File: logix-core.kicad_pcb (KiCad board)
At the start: 6 copper layers, 100 x 80 mm, 238 parts, among them J1 QSH-030-01-X-D-A-XX, J2 QSH-030-01-X-D-A-XX, J3 878321420, Q1 TPNTK3139PT1G, Q10 TPNTK3139PT1G, Q11 2N7002M3T5G-ES, Q12 2N7002M3T5G-ES, Q13 2N7002M3T5G-ES, Q14 2N7002M3T5G-ES, Q15 2N7002M3T5G-ES, Q16 2N7002M3T5G-ES, Q17 2N7002M3T5G-ES, Q18 2N7002M3T5G-ES, Q19 TPNTK3139PT1G, Q2 2N7002M3T5G-ES, Q20 2N7002M3T5G-ES, Q21 2N7002M3T5G-ES, Q22 2N7002M3T5G-ES, Q23 2N7002M3T5G-ES, Q24 2N7002M3T5G-ES, Q25 2N7002M3T5G-ES, Q26 2N7002M3T5G-ES, Q27 2N7002M3T5G-ES, Q3 2N7002M3T5G-ES, Q4 2N7002M3T5G-ES, Q5 2N7002M3T5G-ES, Q6 2N7002M3T5G-ES, Q7 2N7002M3T5G-ES, Q8 2N7002M3T5G-ES, Q9 2N7002M3T5G-ES, SW1 SMXS-04K-TP, SW2 TS-1187A-B-A-B, SW3 TS-1187A-B-A-B, SW4 TS-1187A-B-A-B, U1 XC7A35T-FGG484, U2 MP5470GL-0000-P, U3 TPUSBLC6-4SC6, U4 FT230XQ, U5 MX25L3233FZN, U6 MT41K256M16TW-107:P

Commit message: did alot of stuff
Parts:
- C1, C14, C15, C28, C29, C42, C43, C65, C71, C81: footprint Capacitor_SMD:C_1210_3225Metric -> Capacitor_SMD:C_1206_3216Metric
- R1, R10, R11, R12, R13, R14, R15, R16, R2, R3, R4, R5, R6, R8, R9: footprint Resistor_SMD:R_0402_1005Metric_Pad0.72x0.64mm_HandSolder -> Resistor_SMD:R_0402_1005Metric
- R20: footprint Capacitor_SMD:C_0402_1005Metric -> Resistor_SMD:R_0402_1005Metric
- moved C71 18.0 mm to (140.5, 108.8), turned to 90 degrees
- moved C43 12.0 mm to (173.8, 107.5)
- moved C53 6.15 mm to (126.0, 125.5), turned to -90 degrees
- moved R11 5.71 mm to (125.2, 117.2), turned to 90 degrees
- moved R13 5.26 mm to (125.2, 120.2), turned to -90 degrees
- moved C1 5.14 mm to (178.5, 108.2), turned to 90 degrees
- moved R14 4.10 mm to (128.5, 128.8)
- moved FB1 2.47 mm to (122.2, 115.2)
- moved C14 2.01 mm to (173.8, 104.0)
- moved C8 1.90 mm to (172.2, 101.5)
- moved C9 1.75 mm to (172.2, 100.2)
- moved C13 1.60 mm to (172.2, 99.0)
- moved Q20 1.50 mm to (208.2, 80.0)
- moved Q22 1.50 mm to (209.8, 80.0)
- moved R56 1.50 mm to (208.2, 82.2)
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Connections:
- net Net-(USB1-VCC) renamed /USB/EXT_VBUS
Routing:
- net GND: track 0.00 -> 73.0 mm, vias 0 -> 184
- net (no net): track 0.00 -> 52.7 mm, vias 0 -> 35
- net /DDR3_DQ15: track 0.00 -> 38.4 mm, vias 0 -> 2
- net /DDR3_ADDR8: track 0.00 -> 36.6 mm, vias 0 -> 2
- net /DDR3_UDQS+: track 0.00 -> 36.5 mm, vias 0 -> 2
- net /DDR3_ADDR13: track 0.00 -> 36.4 mm, vias 0 -> 2
- net /DDR3_UDQS-: track 0.00 -> 36.4 mm, vias 0 -> 2
- net /DDR3_ADDR12: track 0.00 -> 34.4 mm, vias 0 -> 2
- net /DDR3_ADDR10: track 0.00 -> 33.6 mm, vias 0 -> 2
- net /DDR3_ADDR11: track 0.00 -> 33.3 mm, vias 0 -> 2
- net /DDR3_DQ10: track 0.00 -> 32.2 mm, vias 0 -> 2
- net /DDR3_ADDR14: track 0.00 -> 31.8 mm, vias 0 -> 2
- net /DDR3_DQ12: track 0.00 -> 31.0 mm, vias 0 -> 2
- net /DDR3_DQ14: track 0.00 -> 30.7 mm, vias 0 -> 2
- net /DDR3_DQ8: track 0.00 -> 29.6 mm, vias 0 -> 2
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- added copper zone on B.Cu, net /FPGA/FPGA pg.1/VCCO13
- added copper zone on F.Cu, net /FPGA/FPGA pg.1/VCCO13
- added copper zone on B.Cu, net /FPGA/FPGA pg.1/VCCO14
- added copper zone on F.Cu, net /FPGA/FPGA pg.1/VCCO14
- added copper zone on B.Cu, net /FPGA/FPGA pg.2/VCCO15
- added copper zone on F.Cu, net /FPGA/FPGA pg.2/VCCO15
- added copper zone on B.Cu, net /FPGA/FPGA pg.2/VCCO16
- added copper zone on F.Cu, net /FPGA/FPGA pg.2/VCCO16
- added copper zone on B.Cu, net /FPGA/FPGA pg.3/VCCO34
- added copper zone on F.Cu, net /FPGA/FPGA pg.3/VCCO34
- added copper zone on B.Cu, net /FPGA/FPGA pg.3/VCCO35
- added copper zone on F.Cu, net /FPGA/FPGA pg.3/VCCO35
- added copper zone on B.Cu, net /FPGA/FPGA pg.4/VCCO_0
- added copper zone on F.Cu, net /FPGA/FPGA pg.4/VCCO_0
- added copper zone on B.Cu, net /FPGA/FPGA pg.5/MGTAVCC
- added copper zone on F.Cu, net /FPGA/FPGA pg.5/MGTAVCC
- added copper zone on B.Cu, net /FPGA/FPGA pg.5/MGTAVTT
- added copper zone on F.Cu, net /FPGA/FPGA pg.5/MGTAVTT
- added copper zone on B.Cu, net /FPGA/FPGA pg.5/VCCADC
- added copper zone on F.Cu, net /FPGA/FPGA pg.5/VCCADC
- added copper zone on B.Cu, net /FPGA/FPGA pg.5/VCCAUX
- added copper zone on F.Cu, net /FPGA/FPGA pg.5/VCCAUX
- added copper zone on B.Cu, net /FPGA/FPGA pg.5/VCCBRAM
- added copper zone on F.Cu, net /FPGA/FPGA pg.5/VCCBRAM
- added copper zone on B.Cu, net /FPGA/FPGA pg.5/VCCINT
- added copper zone on F.Cu, net /FPGA/FPGA pg.5/VCCINT
- added copper zone on F.Cu, net /USB/EXT_VBUS
- added copper zone on B.Cu, net GND
- added copper zone on F.Cu, net GND
- removed copper zone on In4.Cu, net +1V5

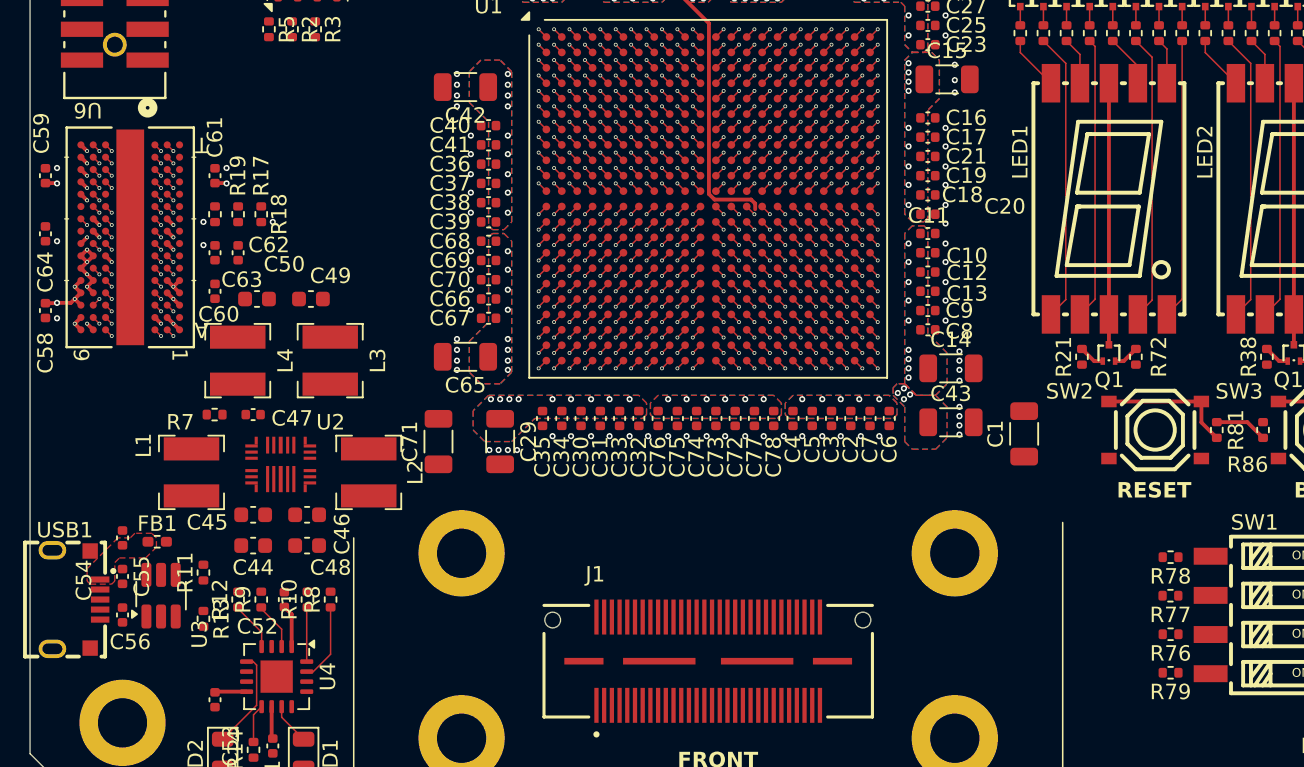
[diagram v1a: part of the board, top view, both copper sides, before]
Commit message: did a bit of ddr routing
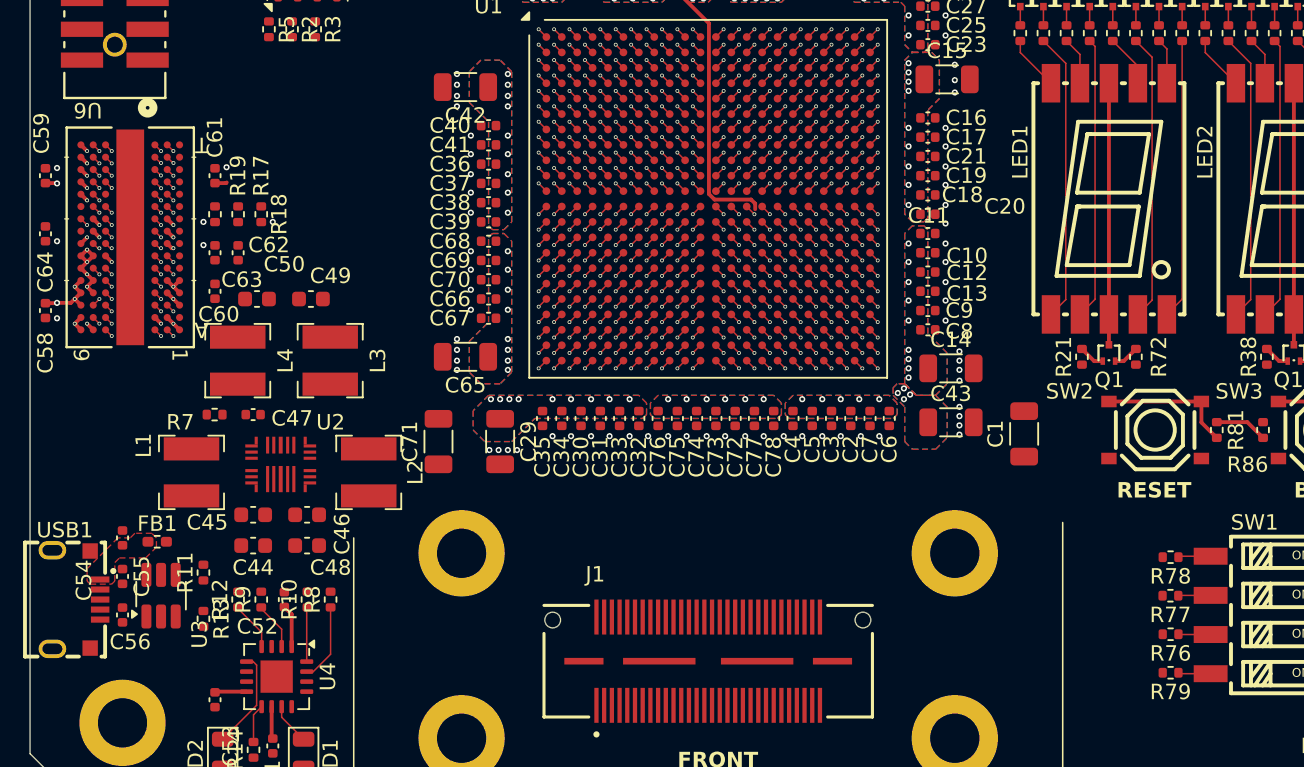
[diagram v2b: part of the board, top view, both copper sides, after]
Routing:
- net /DDR3_BLOCK_ADDR1: track 1.27 -> 42.0 mm
- net /DDR3_LDQS-: track 1.27 -> 40.7 mm
- net /DDR3_DQ7: track 1.27 -> 38.5 mm
- net /DDR3_LDQS+: track 1.27 -> 37.5 mm
- net /DDR3_CLK_EN: track 1.27 -> 36.6 mm
- net /DDR3_DQ5: track 1.27 -> 36.5 mm
- net /DDR3_ADDR4: track 1.27 -> 34.9 mm
- net /DDR3_BLOCK_ADDR2: track 1.27 -> 34.1 mm
- net /DDR3_ADDR6: track 1.27 -> 33.7 mm
- net /DDR3_DQ3: track 1.27 -> 32.5 mm
- net /DDR3_DQ4: track 1.27 -> 31.9 mm
- net /DDR3_ADDR1: track 1.27 -> 31.8 mm
- net /DDR3_DQ6: track 1.27 -> 31.2 mm
- net /DDR3_DQ1: track 1.27 -> 30.5 mm
- net /DDR3_BLOCK_ADDR0: track 1.27 -> 29.4 mm
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
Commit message: did alot of ddr3 routing
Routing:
- net /DDR3_LDM: track 1.27 -> 37.2 mm
- net /DDR3_ODT: track 0.71 -> 27.5 mm, vias 1 -> 2
- net /DDR3_UDM: track 1.27 -> 26.4 mm
- net /DDR3_RAS#: track 16.9 -> 1.27 mm
- net /DDR3_CLK-: track 22.5 -> 33.8 mm
- net /DDR3_CLK+: track 22.5 -> 33.8 mm
- net /DDR3_DQ8: track 29.6 -> 39.5 mm
- net /DDR3_DQ15: track 38.4 -> 30.4 mm
- net /DDR3_ADDR13: track 36.4 -> 29.7 mm
- net /DDR3_BLOCK_ADDR1: track 42.0 -> 47.6 mm
- net /DDR3_UDQS-: track 36.4 -> 32.0 mm
- net /DDR3_ADDR2: track 28.2 -> 31.8 mm
- net /DDR3_UDQS+: track 36.5 -> 32.9 mm
- net /DDR3_ADDR14: track 31.8 -> 35.2 mm
- net /DDR3/ZQ: track 11.9 -> 8.88 mm
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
